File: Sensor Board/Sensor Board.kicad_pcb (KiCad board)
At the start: 2 copper layers, 34 parts, among them J1 Programming Header, J2 Irradience Sensor, J3 Micro_SD_Card, J4 CAN Bus Connector, U1 PIC18F26K83, U2 INA180, U4 MCP2562, U5 INA180, Y1 12MHz Crystal

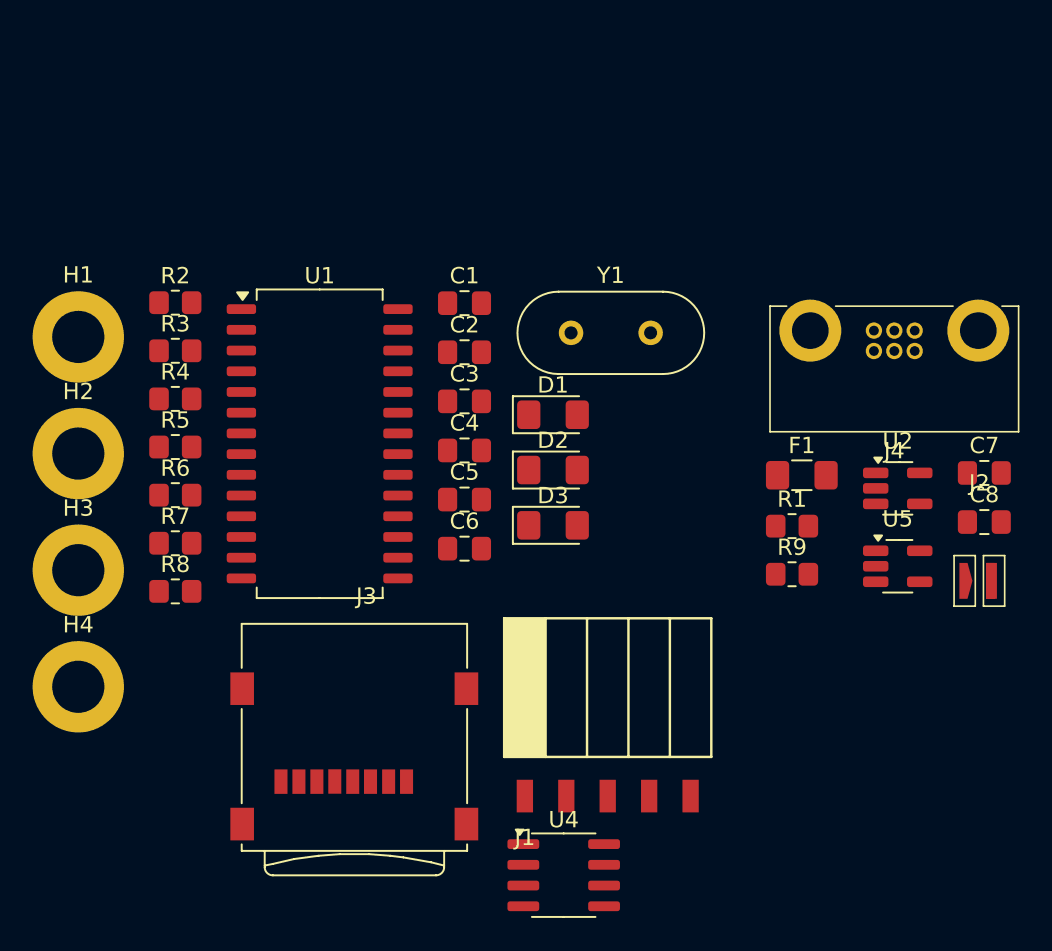
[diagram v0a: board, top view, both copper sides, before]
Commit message: Change 3.3v on sensor
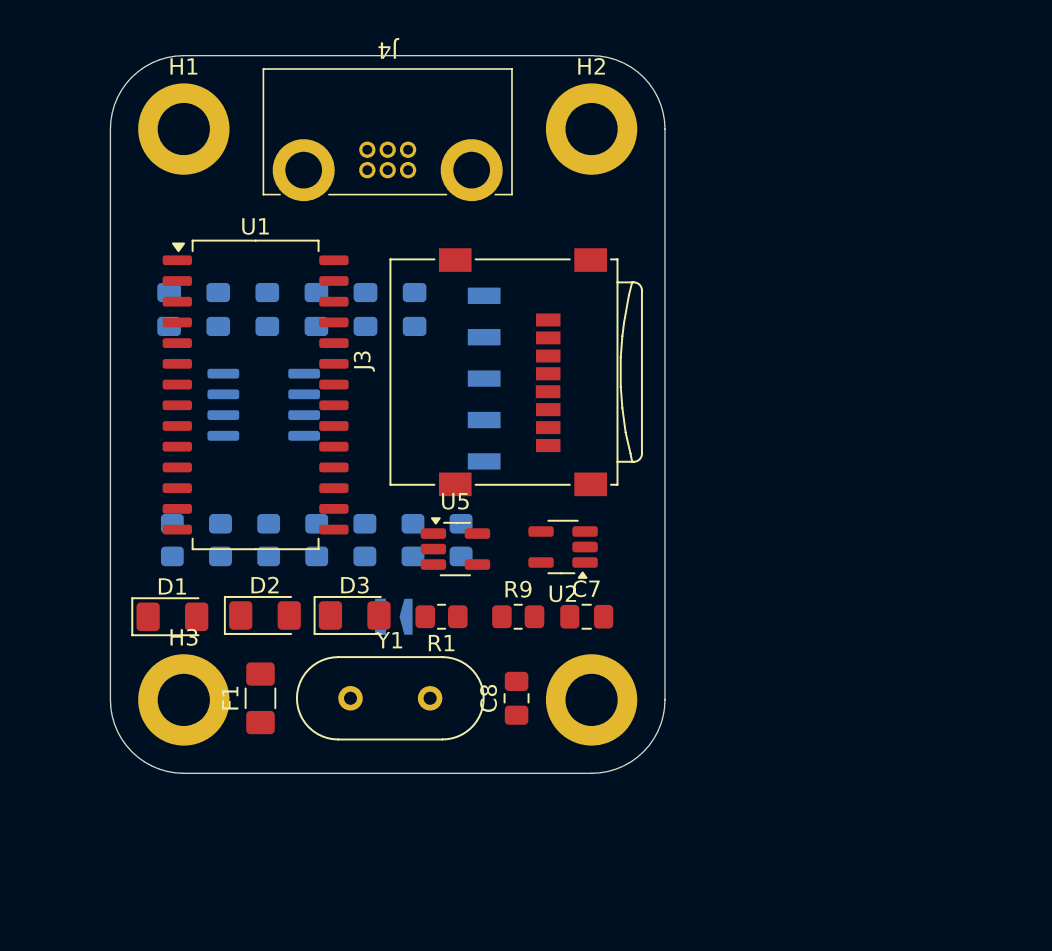
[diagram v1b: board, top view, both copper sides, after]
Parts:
- C1, C2, C3, C4, C5, C6, J1, J2, R2, R3, R4, R5, R6, R7, R8, U4: moved to B.Cu
- moved H2 37.2 mm to (155.0, 60.0)
- moved J2 36.0 mm to (142.8, 89.9), turned to 180 degrees
- moved F1 35.9 mm to (134.7, 94.9), turned to 90 degrees
- moved U4 34.2 mm to (134.9, 76.9)
- moved J4 32.6 mm to (142.5, 62.5), turned to 180 degrees
- moved H4 31.5 mm to (155.0, 95.0)
- moved C8 30.6 mm to (150.4, 94.9), turned to 90 degrees
- moved J3 29.8 mm to (154.9, 81.8), turned to 90 degrees
- moved U5 27.1 mm to (146.7, 85.8)
- moved D1 26.4 mm to (129.3, 89.9)
- moved Y1 26.2 mm to (140.2, 94.9)
- moved C7 25.9 mm to (154.7, 89.9)
- moved C6 23.3 mm to (129.1, 71.1), turned to 90 degrees
- moved R1 22.2 mm to (145.8, 89.9), turned to 180 degrees
- moved U2 20.8 mm to (153.2, 85.6), turned to 180 degrees
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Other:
- board outline added: 34 x 44 mm
